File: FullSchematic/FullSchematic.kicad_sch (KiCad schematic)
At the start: 21 parts, among them J1 USB_A, J2 ATX-24, J3 Red Banana Jack, J4 Black Banana Jack, J5 2x6 Pin Header, J6 2x6 Pin Header, J7 CT3151-2, J8 CT3151-2, Q1 BSS138-7-F, SW1 Rotary Switch

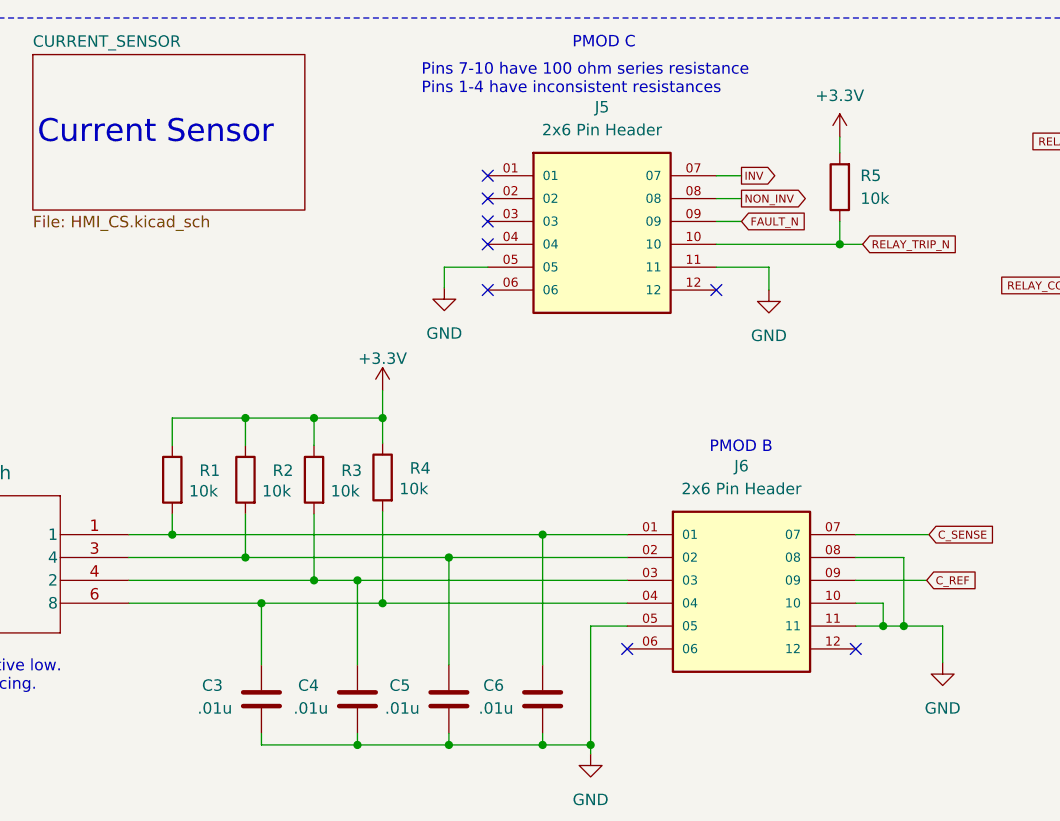
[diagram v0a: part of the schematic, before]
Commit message: Schematic/Footprint Update
Corrected Footprint / Schematic for PCB Design and Changed 10k Resistors to 0603 size.
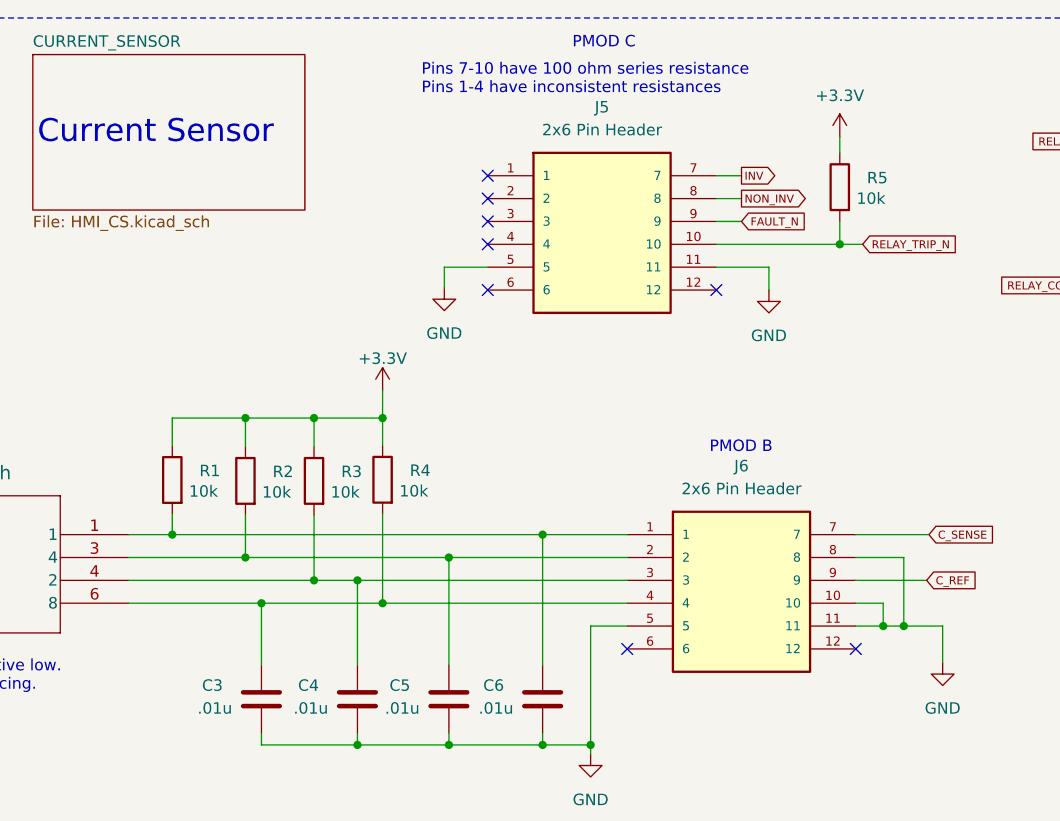
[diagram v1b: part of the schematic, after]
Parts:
- R1, R2, R3, R4, R5: footprint Resistor_SMD:R_1206_3216Metric -> Resistor_SMD:R_0201_0603Metric; MFG P/N CRCW120610K0FKEA -> CRCW060310K0FKEB; SEL P/N 255-1002 -> 252-1002
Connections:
- net +3.3V: now also R5.1; no longer R5.2
- net C_REF: now also J6.9; no longer J6.09
- net C_SENSE: now also J6.7; no longer J6.07
- net FAULT_N: now also J5.9; no longer J5.09
- net GND: now also J5.5, J6.5, J6.8; no longer J5.05, J6.05, J6.08
- net INV: now also J5.7; no longer J5.07
- net NON_INV: now also J5.8; no longer J5.08
- net RELAY_TRIP_N: now also R5.2; no longer R5.1
- net at C5.1, R2.2, SW1.3 (4): now also J6.2; no longer J6.02
- net at C6.1, R1.2, SW1.1: now also J6.1; no longer J6.01
- net at C4.1, R3.2, SW1.4 (2): now also J6.3; no longer J6.03
- net at C3.1, R4.2, SW1.6 (8): now also J6.4; no longer J6.04

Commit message: More Edits
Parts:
- added R11: 33k, Resistor_SMD:R_0603_1608Metric, symbol Device:R
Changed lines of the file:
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@@
+    )
+  )
+  (symbol (lib_id "Device:R") (at 105.664 34.798 0) (unit 1)
+    (in_bom yes) (on_board yes) (dnp no) (fields_autoplaced)
+    (property "Reference" "R11" (at 107.696 33.528 0)
+      (effects (font (size 1.27 1.27)) (justify left))
+    )
+    (property "Value" "33k" (at 107.696 36.068 0)
+      (effects (font (size 1.27 1.27)) (justify left))
+    )
+    (property "Footprint" "Resistor_SMD:R_0603_1608Metric" (at 103.886 34.798 90)
+      (effects (font (size 1.27 1.27)) hide)
+    )
+    (property "Datasheet" "~" (at 105.664 34.798 0)
+      (effects (font (size 1.27 1.27)) hide)
+    )
+    (property "SEL P/N" "462-33K0 " (at 105.664 34.798 0)
+      (effects (font (size 1.27 1.27)) hide)
+    )
+    (property "MFG P/N" "RMCF0603JT33K0" (at 105.664 34.798 0)
+      (effects (font (size 1.27 1.27)) hide)
+    )
+    (pin "1")
+    (pin "2")
+    (instances
+      (project "FullSchematic"
+        (path "/650f0e66-3493-4c97-9577-99f99fcd23df/3542ca37-4624-4740-af78-19651a951512"
+          (reference "R11") (unit 1)
+        )
+        (path "/650f0e66-3493-4c97-9577-99f99fcd23df"
+          (reference "R11") (unit 1)
+        )
+      )
+      (project "Senior Design HMI Schematic R2 20230722_MB"
+        (path "/8c847d65-180e-4b65-a3db-30ced04c6f38"
+          (reference "R19") (unit 1)
+        )
+        (path "/8c847d65-180e-4b65-a3db-30ced04c6f38/74cc473d-d4c1-4a03-a7be-fcad9d3b3420"
+          (reference "R10") (unit 1)
+        )
+      )
     )
   )

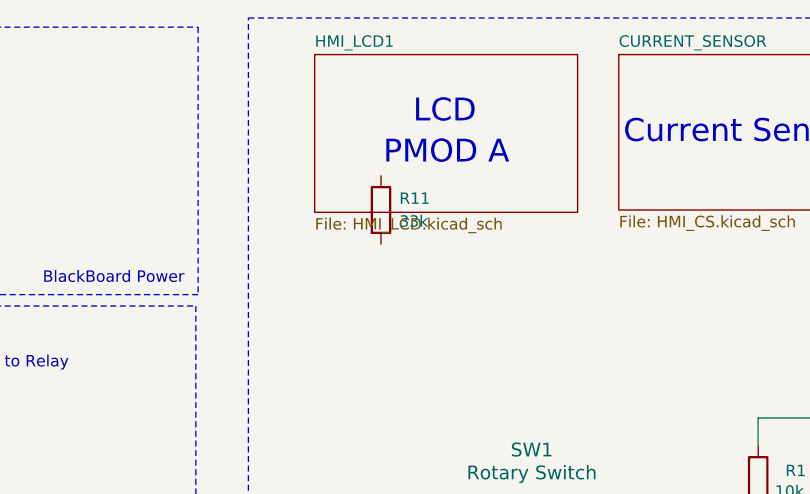
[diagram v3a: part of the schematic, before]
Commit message: Corrected trace size for high current
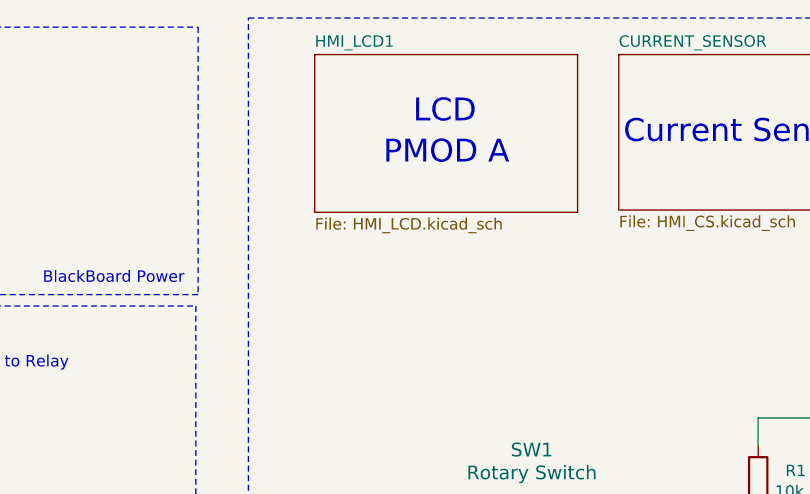
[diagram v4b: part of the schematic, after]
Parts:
- removed R11: 33k, Resistor_SMD:R_0603_1608Metric, symbol Device:R
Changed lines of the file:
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@@
-    )
-  )
-  (symbol (lib_id "Device:R") (at 105.664 34.798 0) (unit 1)
-    (in_bom yes) (on_board yes) (dnp no) (fields_autoplaced)
-    (property "Reference" "R11" (at 107.696 33.528 0)
-      (effects (font (size 1.27 1.27)) (justify left))
-    )
-    (property "Value" "33k" (at 107.696 36.068 0)
-      (effects (font (size 1.27 1.27)) (justify left))
-    )
-    (property "Footprint" "Resistor_SMD:R_0603_1608Metric" (at 103.886 34.798 90)
-      (effects (font (size 1.27 1.27)) hide)
-    )
-    (property "Datasheet" "~" (at 105.664 34.798 0)
-      (effects (font (size 1.27 1.27)) hide)
-    )
-    (property "SEL P/N" "462-33K0 " (at 105.664 34.798 0)
-      (effects (font (size 1.27 1.27)) hide)
-    )
-    (property "MFG P/N" "RMCF0603JT33K0" (at 105.664 34.798 0)
-      (effects (font (size 1.27 1.27)) hide)
-    )
-    (pin "1")
-    (pin "2")
-    (instances
-      (project "FullSchematic"
-        (path "/650f0e66-3493-4c97-9577-99f99fcd23df/3542ca37-4624-4740-af78-19651a951512"
-          (reference "R11") (unit 1)
-        )
-        (path "/650f0e66-3493-4c97-9577-99f99fcd23df"
-          (reference "R11") (unit 1)
-        )
-      )
-      (project "Senior Design HMI Schematic R2 20230722_MB"
-        (path "/8c847d65-180e-4b65-a3db-30ced04c6f38"
-          (reference "R19") (unit 1)
-        )
-        (path "/8c847d65-180e-4b65-a3db-30ced04c6f38/74cc473d-d4c1-4a03-a7be-fcad9d3b3420"
-          (reference "R10") (unit 1)
-        )
-      )
     )
   )

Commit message: Semi-complete board
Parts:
- J5, J6: footprint Connector_PinHeader_2.54mm:PinHeader_2x06_P2.54mm_Vertical -> CustomFootprints:PMOD
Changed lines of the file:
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@@
-    (stroke (width 0) (type default))
-  )
-  (wire (pts (xy 182.626 41.148) (xy 177.8 41.148))
     (stroke (width 0) (type default))
   )
@@
   )
   (wire (pts (xy 260.096 40.64) (xy 258.572 40.64))
+    (stroke (width 0) (type default))
+  )
+  (wire (pts (xy 177.8 41.148) (xy 182.626 41.148))
     (stroke (width 0) (type default))
   )
@@
   )
   (text "Pins 7-10 have 100 ohm series resistance\nPins 1-4 have inconsistent resistances\n"
-    (at 175.26 22.098 0)
+    (at 191.77 61.976 0)
     (effects (font (size 1.27 1.27)) (justify left bottom))
   )
@@
     (effects (font (size 1.27 1.27)) (justify left bottom))
   )
-  (text "PMOD B\n" (at 207.264 61.976 0)
+  (text "PMOD B\n" (at 192.024 21.844 0)
     (effects (font (size 1.27 1.27)) (justify left bottom))
   )
@@
     (effects (font (size 2.54 2.54)) (justify left bottom))
   )
-  (text "PMOD C\n" (at 192.024 17.018 0)
+  (text "PMOD C\n" (at 208.534 56.896 0)
     (effects (font (size 1.27 1.27)) (justify left bottom))
   )
@@
       (effects (font (size 1.27 1.27)))
     )
-    (property "Footprint" "Connector_PinHeader_2.54mm:PinHeader_2x06_P2.54mm_Vertical" (at 211.5312 88.646 0)
+    (property "Footprint" "CustomFootprints:PMOD" (at 211.5312 88.646 0)
       (effects (font (size 1.27 1.27)) (justify bottom) hide)
     )
@@
   )
   (symbol (lib_name "SFMC-106-L2-L-D_2") (lib_id "SFMC-106-L2-L-D:SFMC-106-L2-L-D") (at 195.326 38.608 0) (unit 1)
-    (in_bom yes) (on_board yes) (dnp no) (fields_autoplaced)
+    (in_bom yes) (on_board yes) (dnp no)
     (property "Reference" "J5" (at 195.326 23.368 0)
       (effects (font (size 1.27 1.27)))
@@
       (effects (font (size 1.27 1.27)))
     )
-    (property "Footprint" "Connector_PinHeader_2.54mm:PinHeader_2x06_P2.54mm_Vertical" (at 196.0372 48.768 0)
+    (property "Footprint" "CustomFootprints:PMOD" (at 196.0372 48.768 0)
       (effects (font (size 1.27 1.27)) (justify bottom) hide)
     )

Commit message: PCB V.4
Fixed power plane issues, cleaned up silk screen, cleaned up via stitching, changed ATX connector to one perpendicular with the board.
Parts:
- J2: footprint CustomFootprints:CON_39291247 -> CustomFootprints:CONN_442060001_MOL; MFG P/N 39291247 -> 442060001
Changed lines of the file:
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@@
       (effects (font (size 1.524 1.524)) (justify left))
     )
-    (property "Footprint" "CustomFootprints:CON_39291247" (at 37.338 109.728 0)
+    (property "Footprint" "CustomFootprints:CONN_442060001_MOL" (at 37.338 109.728 0)
       (effects (font (size 1.27 1.27) italic) hide)
     )
@@
       (effects (font (size 1.27 1.27)) hide)
     )
-    (property "MFG P/N" "39291247" (at 38.354 112.268 0)
+    (property "MFG P/N" "442060001" (at 38.354 112.268 0)
       (effects (font (size 1.27 1.27)) hide)
     )
